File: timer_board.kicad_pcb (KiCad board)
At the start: 2 copper layers, 127 x 76.2 mm, 54 parts, among them CON1 AVR-ISP-6, IC1 ATMEGA32U4, K1 T9AS5D22-5, P1 USBMICRO, P2 OUT_INV, P3 Trigger, P4 OUT, Q1 NPN, Q2 NPN, U1 DS3231MZ, U2 74HC04, Y1 RESONATORSMD

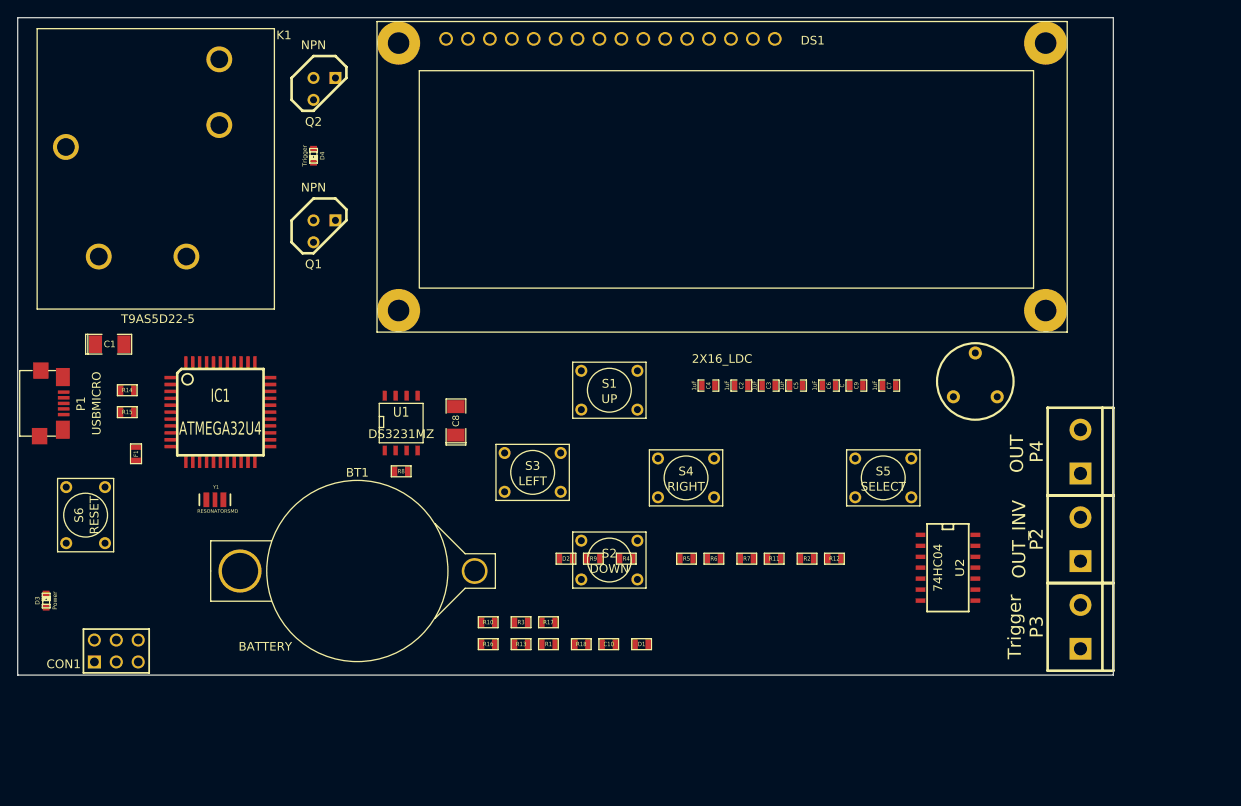
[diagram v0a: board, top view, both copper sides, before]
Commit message: Moved resistors arround
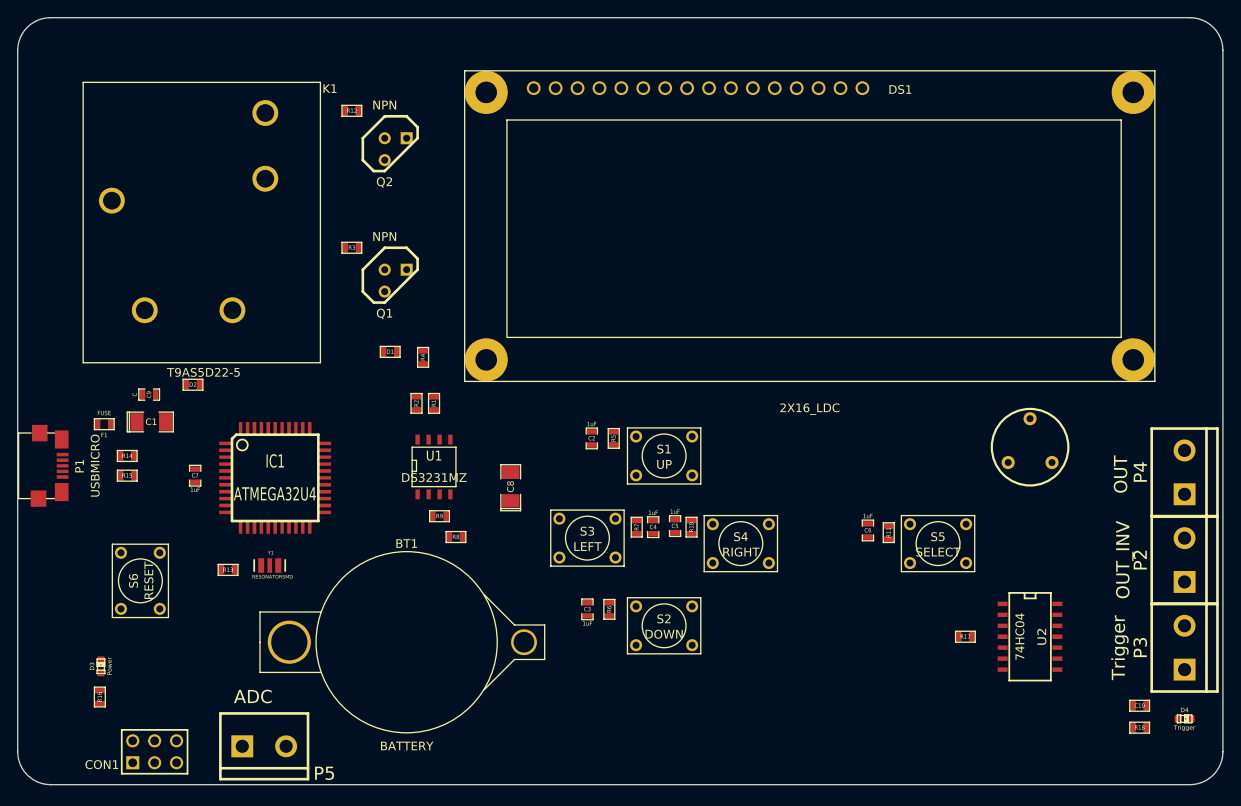
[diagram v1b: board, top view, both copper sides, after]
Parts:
- added P5: ADC, bornier2, F.Cu at (54.0, 109.9)
- moved D4 120.2 mm to (160.7, 106.7), turned to 0 degrees
- moved C9 82.0 mm to (40.6, 69.1)
- moved C7 81.1 mm to (46.0, 78.5), turned to 90 degrees
- moved R12 76.3 mm to (64.1, 36.2), turned to 180 degrees
- moved R18 65.4 mm to (155.4, 107.7), turned to 180 degrees
- moved C10 62.0 mm to (155.4, 105.2)
- moved R2 48.7 mm to (71.6, 70.1), turned to 270 degrees
- moved R17 48.4 mm to (135.3, 97.2)
- moved D2 47.7 mm to (45.7, 67.9), turned to 180 degrees
- moved R3 47.6 mm to (64.1, 52.1)
- moved R16 45.4 mm to (34.9, 104.1), turned to 270 degrees
- moved D1 44.7 mm to (68.6, 64.1), turned to 180 degrees
- moved R13 35.0 mm to (49.8, 89.4), turned to 180 degrees
- moved C3 33.4 mm to (91.4, 94.0), turned to 90 degrees
- moved R4 33.2 mm to (72.4, 64.8), turned to 270 degrees
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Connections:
- IC1 pad 21: (no net) -> OUT
- IC1 pad 41: N-000051 -> N-000037
- U2 pad 5: N-000051 -> OUT
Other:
- board size 127 x 76.2 mm -> 139.7 x 88.9 mm

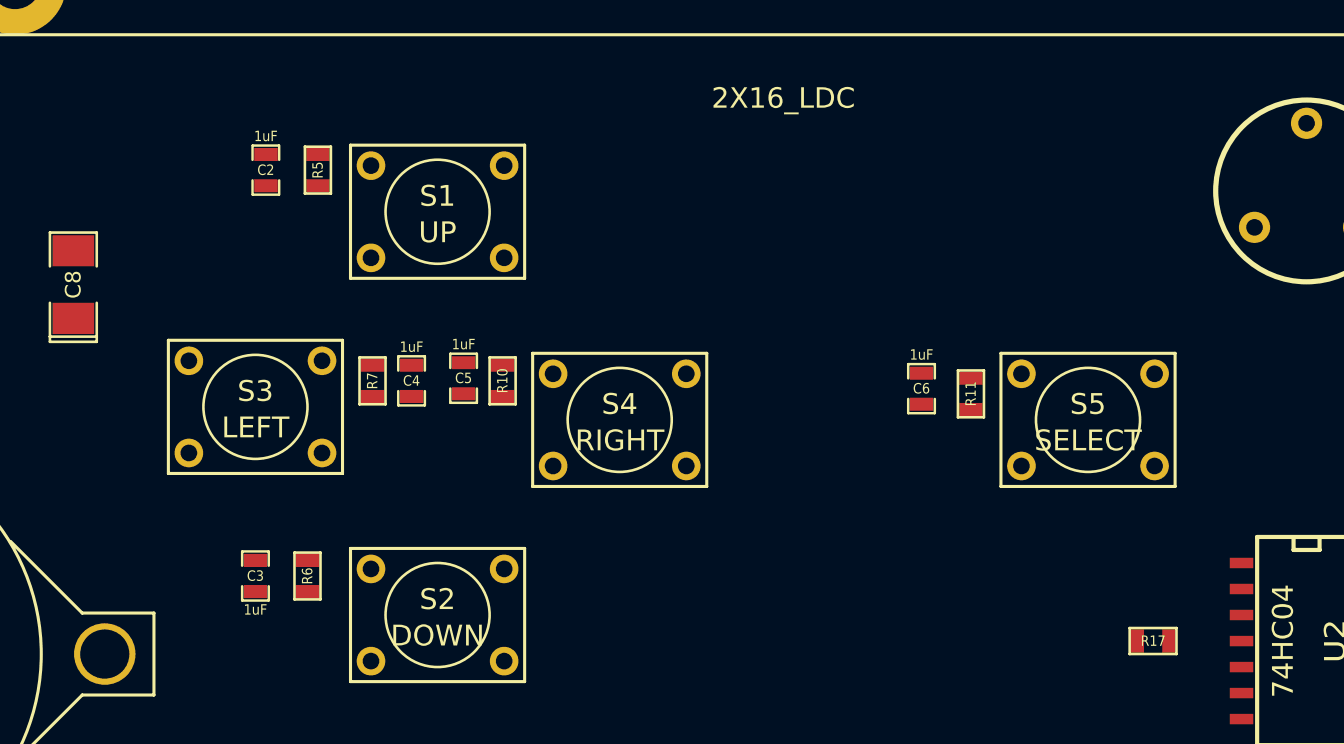
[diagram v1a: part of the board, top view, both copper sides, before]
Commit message: Updated kicad to 4022 and moved resistors
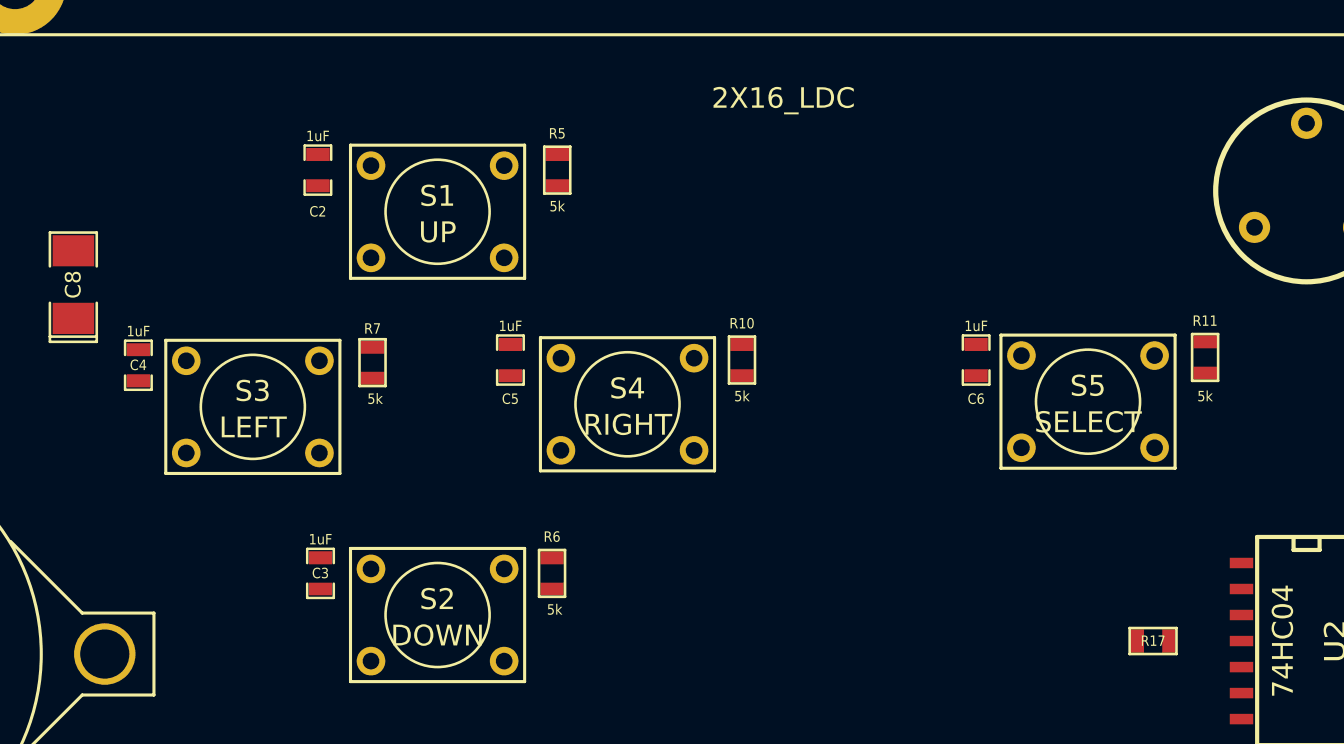
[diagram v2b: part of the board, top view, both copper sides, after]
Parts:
- moved C4 13.4 mm to (85.7, 83.7)
- moved R6 11.9 mm to (105.9, 93.9)
- moved R10 11.7 mm to (115.2, 83.4)
- moved R5 11.7 mm to (106.2, 74.2)
- moved R11 11.6 mm to (137.8, 83.3)
- moved C3 3.18 mm to (94.6, 93.9), turned to 270 degrees
- moved C6 3.01 mm to (126.6, 83.4)
- moved C2 2.54 mm to (94.5, 74.2)
- moved C5 2.45 mm to (103.9, 83.4)
- moved R7 0.89 mm to (97.2, 83.6)
- moved S5 0.89 mm to (132.1, 85.5)
- moved S4 0.85 mm to (109.6, 85.6)
- moved S3 0.13 mm to (91.3, 85.7)

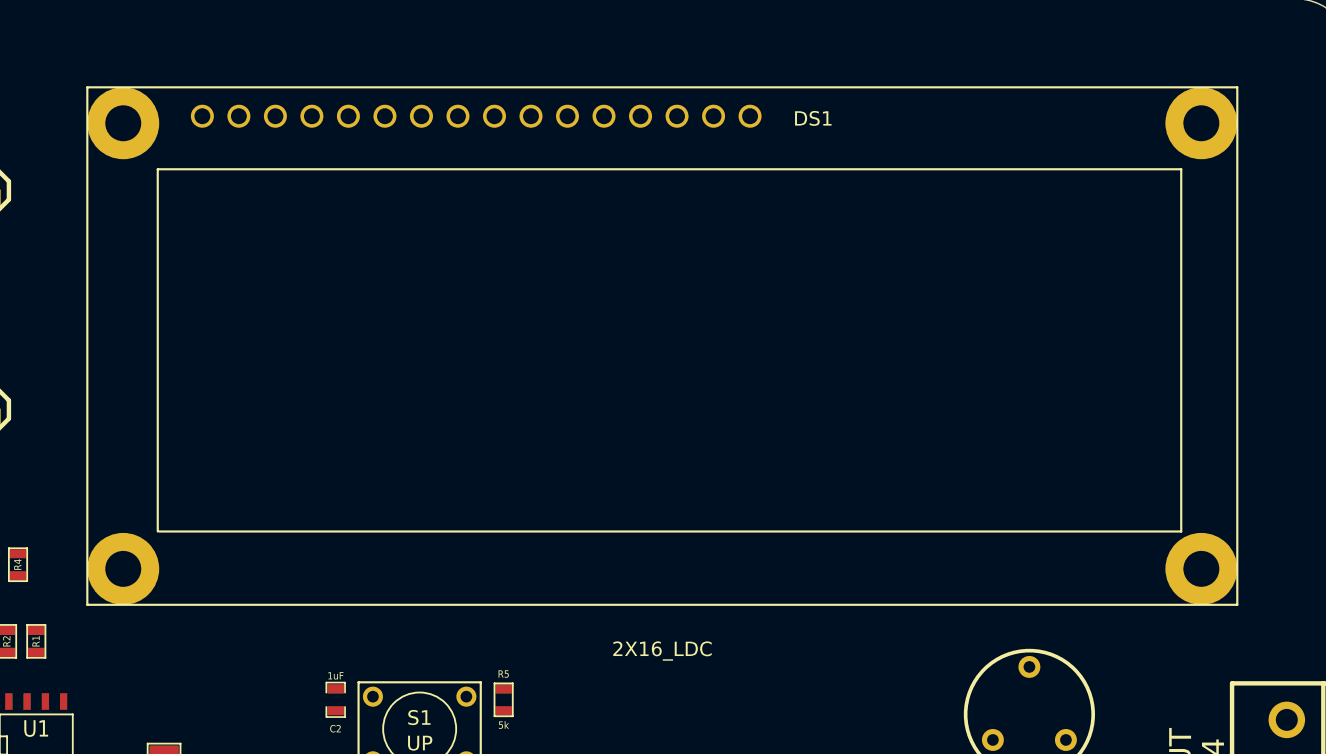
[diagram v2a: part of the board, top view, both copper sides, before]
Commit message: Modified LCD
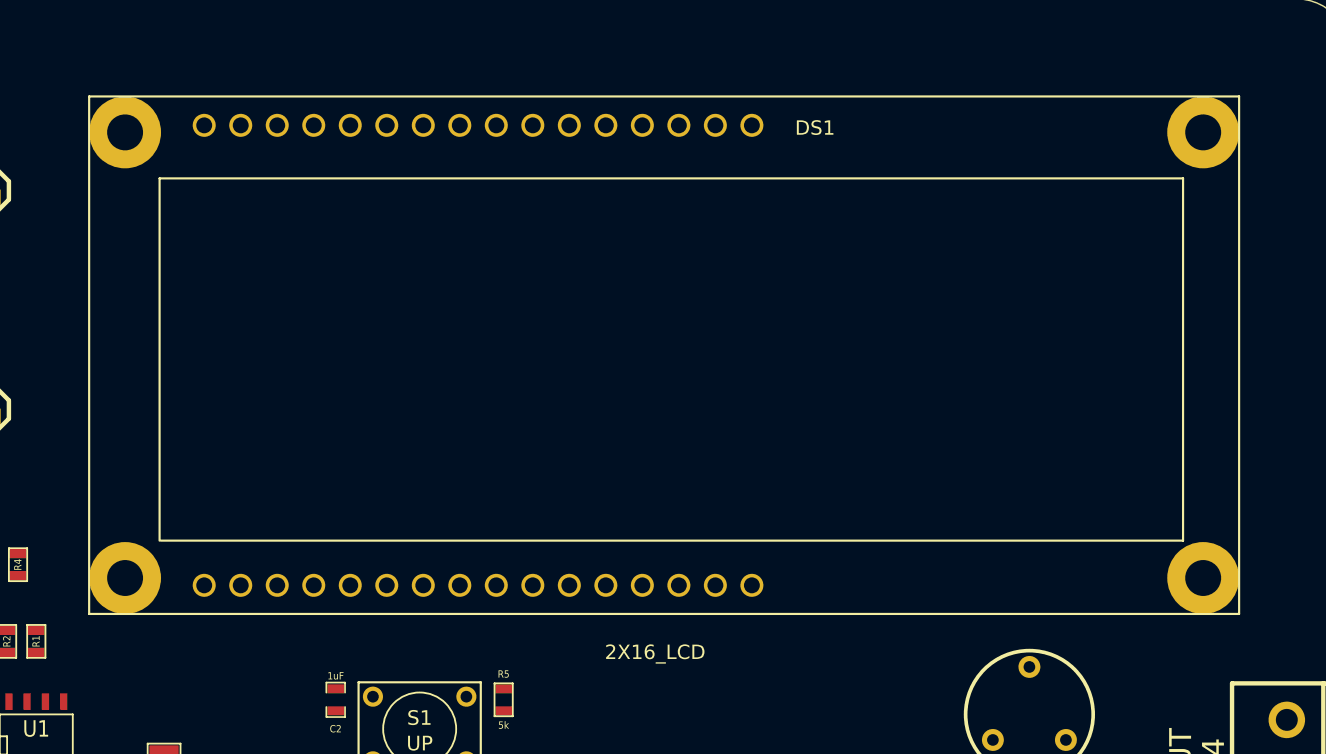
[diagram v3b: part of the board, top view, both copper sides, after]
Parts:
- DS1: value 2X16_LDC -> 2X16_LCD
- moved DS1 0.65 mm to (92.8, 36.2)

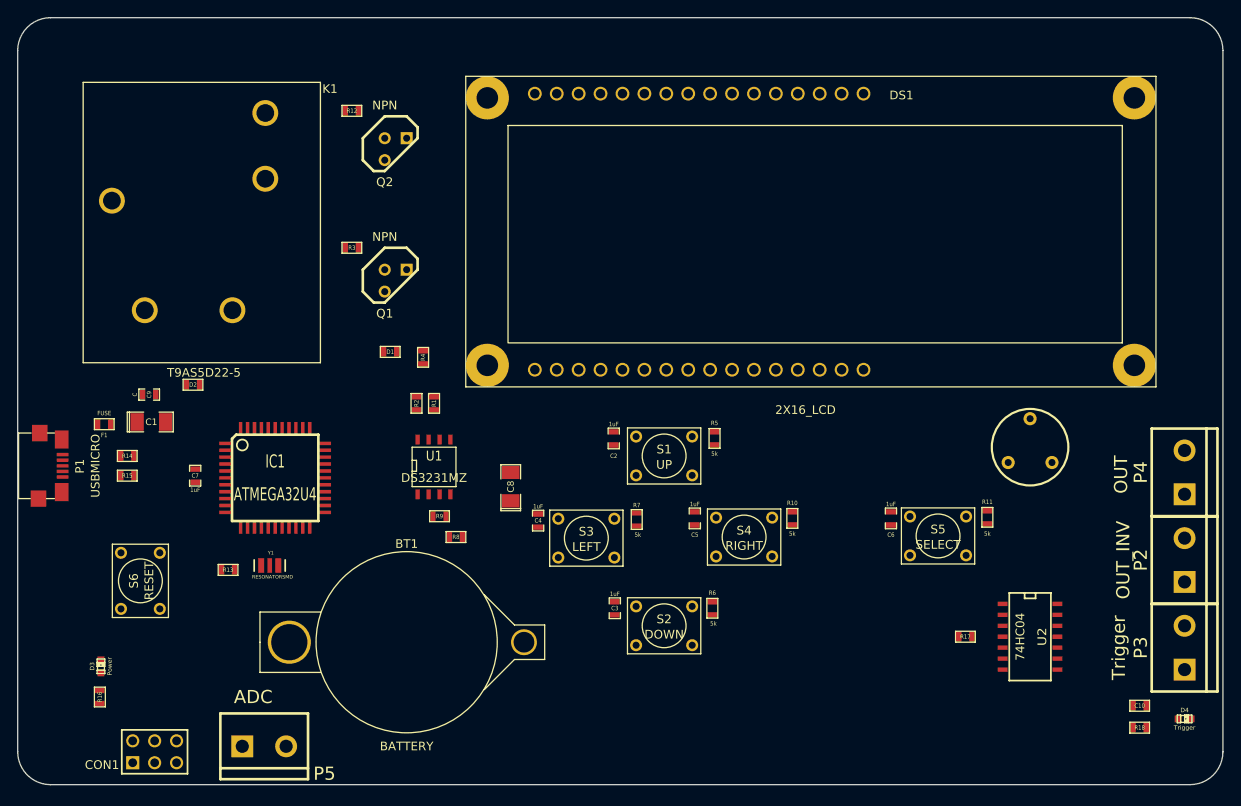
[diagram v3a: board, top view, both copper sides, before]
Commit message: Added test point for 32khz, moved parts arround
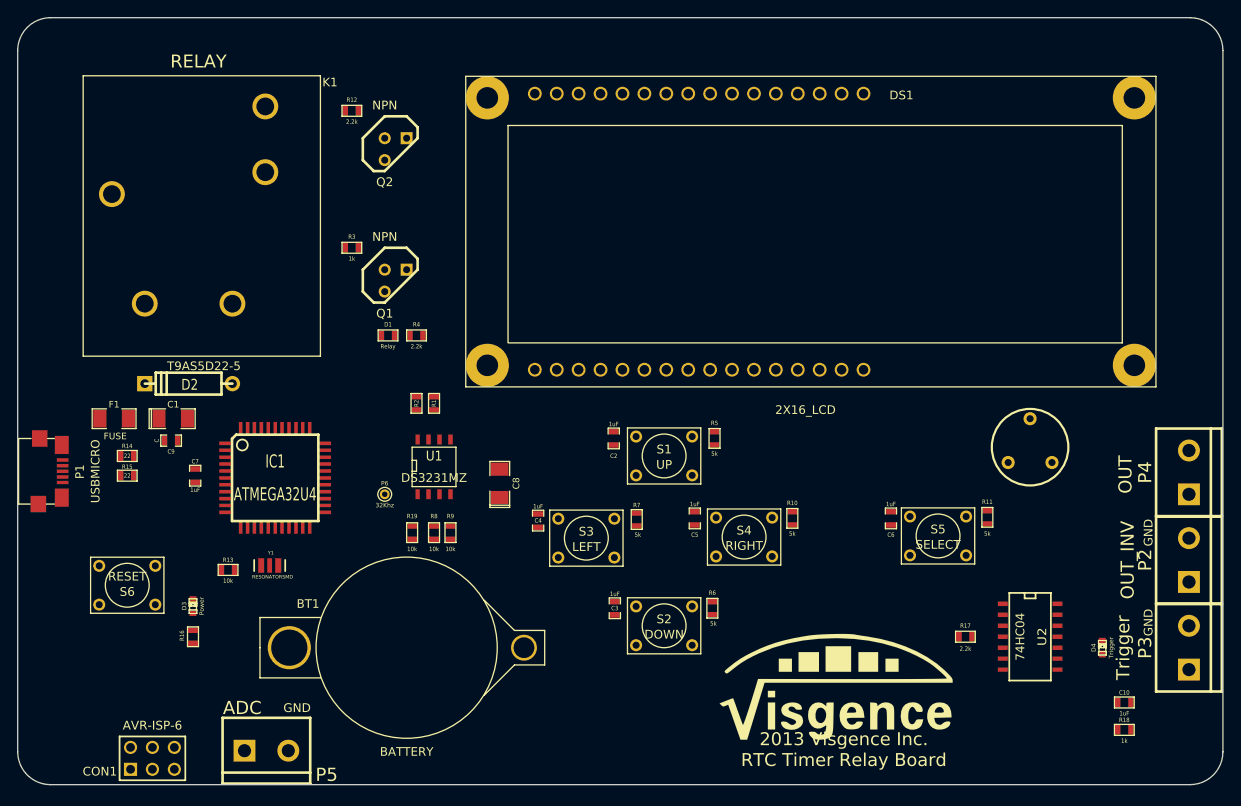
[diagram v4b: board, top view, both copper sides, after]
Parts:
- added G***: LOGO, LOGO, B.Cu at (95.2, 45.1)
- added G1: LOGO, LOGO, F.Cu at (120.4, 103.3)
- added P6: 32Khz, PINTST, F.Cu at (67.9, 80.6)
- added R19: 10k, SM0603, F.Cu at (71.1, 85.1)
- D2: footprint SM0603 -> D4
- F1: footprint SM0603 -> SM1206
- moved R16 12.9 mm to (45.7, 97.2)
- moved D3 12.8 mm to (45.7, 93.6)
- moved D4 12.6 mm to (151.1, 98.4), turned to 90 degrees
- moved C9 5.91 mm to (43.2, 74.4)
- moved R4 2.65 mm to (71.6, 62.2), turned to 0 degrees
- moved R8 2.59 mm to (73.7, 85.1), turned to 90 degrees
- moved C1 2.57 mm to (43.4, 71.9)
- moved R9 2.29 mm to (75.6, 85.1), turned to 90 degrees
- moved D1 1.92 mm to (68.3, 62.2)
- moved C10 1.82 mm to (153.7, 104.8)
- moved R18 1.80 mm to (153.7, 108.0)
- moved S6 1.61 mm to (38.1, 91.2), turned to 180 degrees
- moved C8 1.33 mm to (81.3, 79.4)
- moved F1 1.31 mm to (36.6, 71.9)
- moved CON1 0.80 mm to (41.0, 111.3)
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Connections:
- U1 pad 1: (no net) -> N-000038
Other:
- board text added: "2012 Visgence Inc. RTC Timer Relay Board"
- board text added: "2013 Visgence Inc. RTC Timer Relay Board"
- board text added: "GND"
- board text added: "RELAY"
